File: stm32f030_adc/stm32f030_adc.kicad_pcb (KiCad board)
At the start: 2 copper layers, 35 parts, among them J4 Conn_01x05_Socket, Q1 BC337, U1 STM32F103C6Tx, U2 AMS1117-3.3, X1 USB_B_Micro, Y1 8 MHz

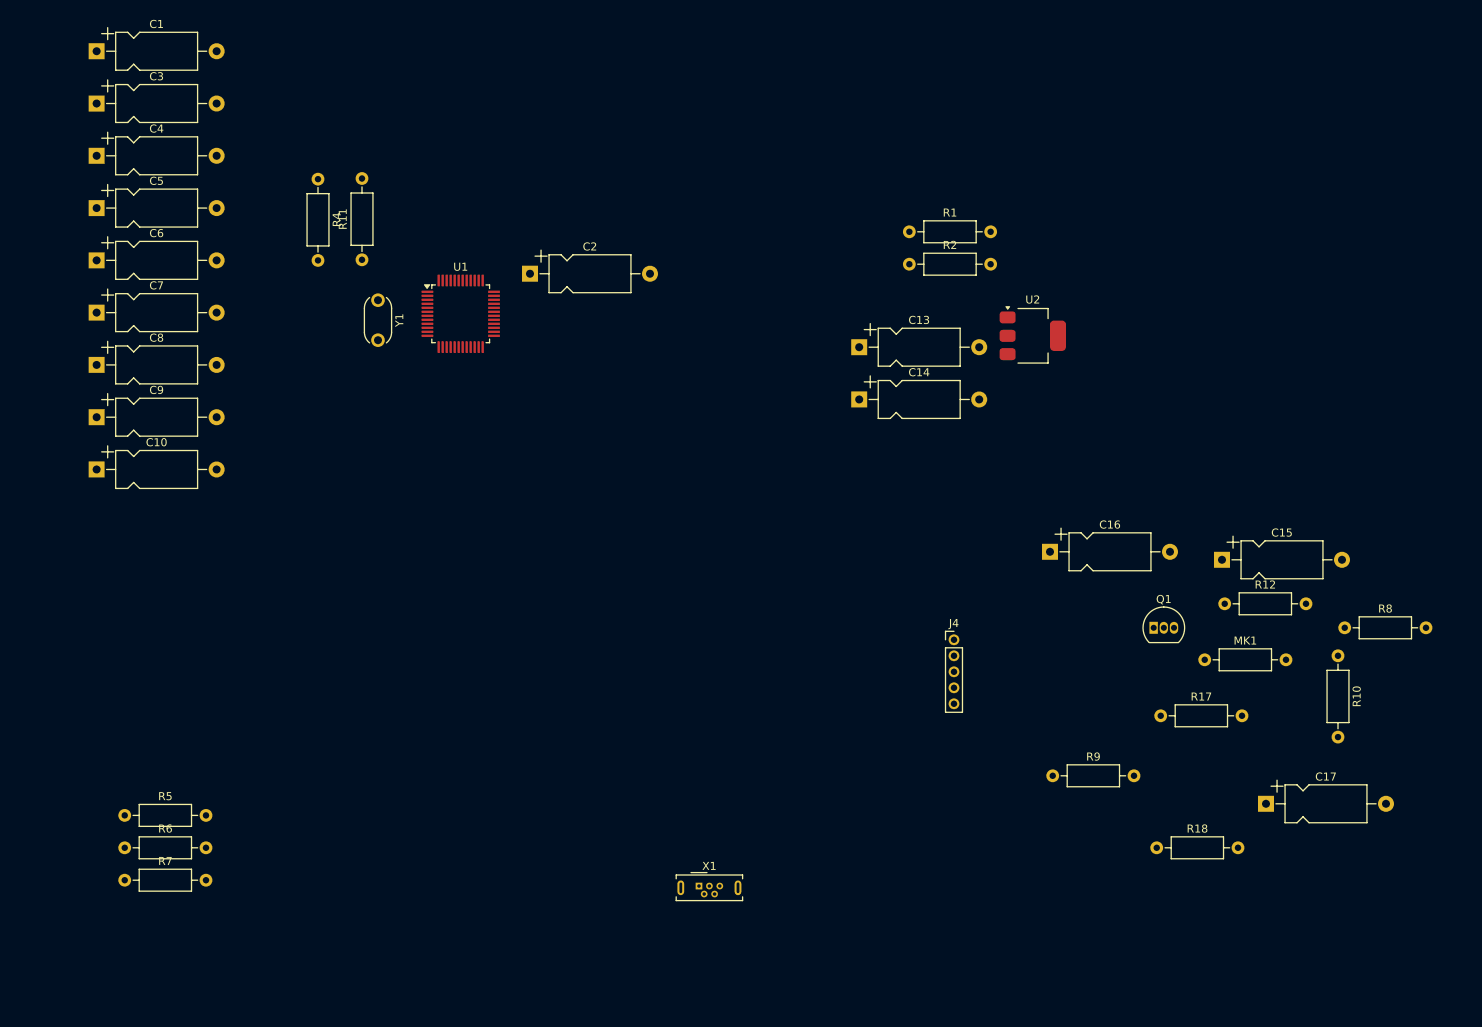
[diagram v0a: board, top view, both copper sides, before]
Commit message: [schematics] Build | Changed oscillator type, fixed unconnected lines, made some layout
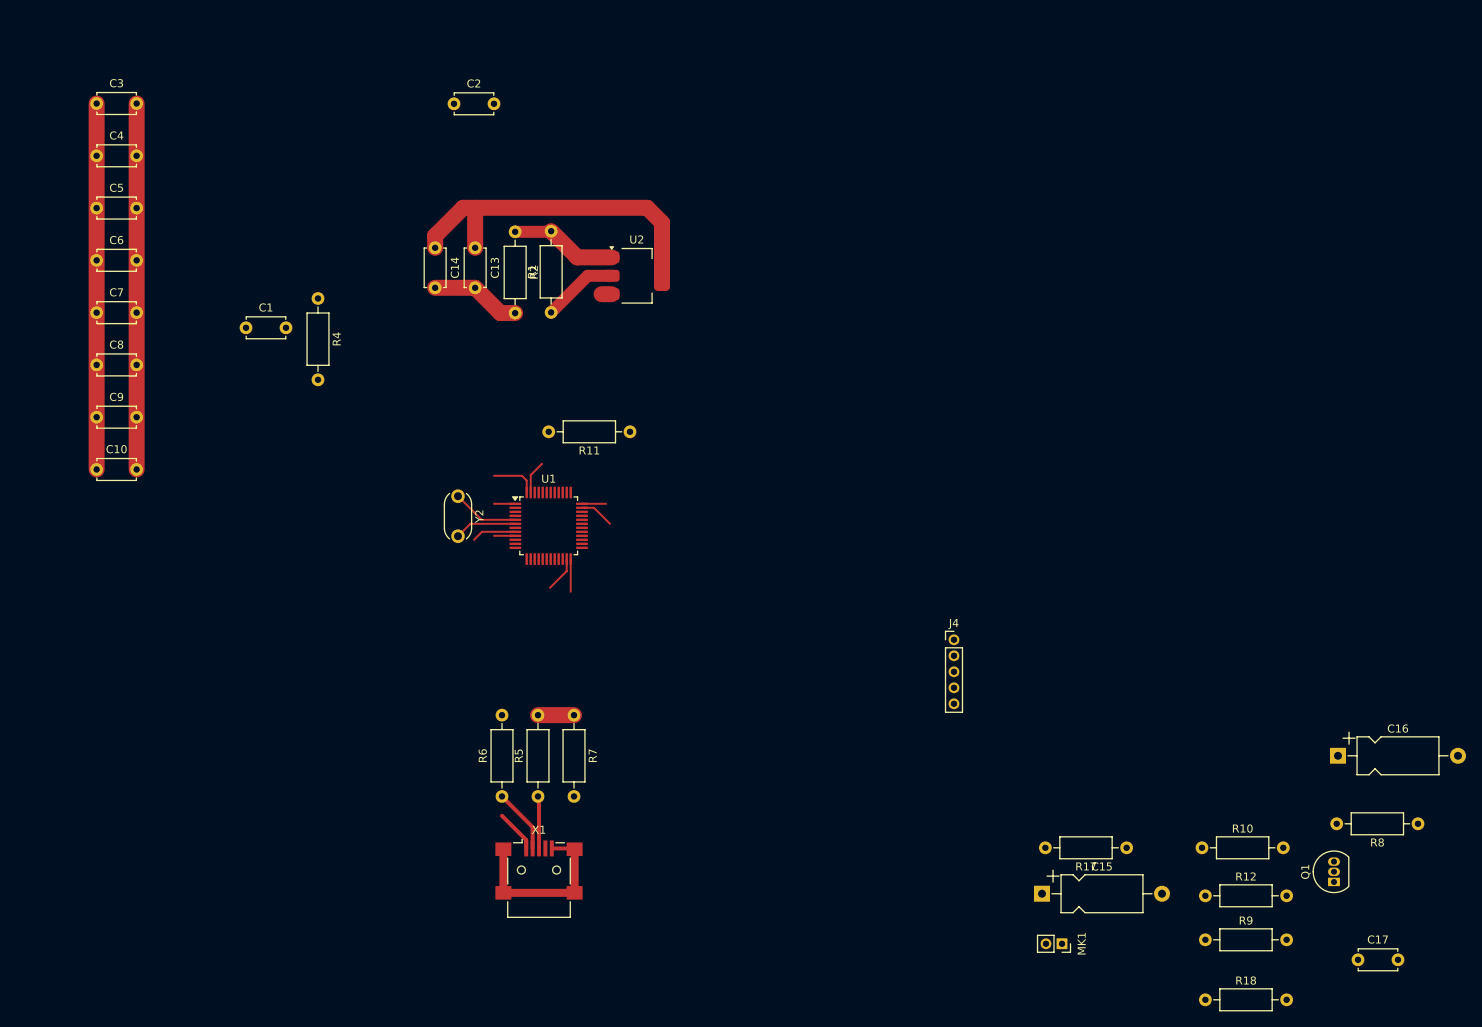
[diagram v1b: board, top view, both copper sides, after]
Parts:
- removed Y1: 8 MHz, Crystal:Resonator-2Pin_W6.0mm_H3.0mm
- added Y2: 8 MHz, Crystal:Resonator-2Pin_W6.0mm_H3.0mm, F.Cu at (142.0, 88.5)
- C1, C10, C13, C14, C17, C2, C3, C4, C5, C6, C7, C8, C9: footprint Capacitor_THT:CP_Axial_L10.0mm_D4.5mm_P15.00mm_Horizontal -> Capacitor_THT:C_Disc_D4.7mm_W2.5mm_P5.00mm
- MK1: footprint Resistor_THT:R_Axial_DIN0207_L6.3mm_D2.5mm_P10.16mm_Horizontal -> Connector_PinSocket_2.00mm:PinSocket_1x02_P2.00mm_Vertical
- X1: footprint Connector_USB:USB_Micro-B_Wuerth_614105150721_Vertical -> Connector_USB:USB_Mini-B_Lumberg_2486_01_Horizontal
- moved R7 59.8 mm to (156.5, 115.9), turned to -90 degrees
- moved C14 56.3 mm to (139.1, 57.5), turned to -90 degrees
- moved R5 51.7 mm to (152.0, 126.1), turned to 90 degrees
- moved U2 50.1 mm to (164.3, 61.0)
- moved C13 49.6 mm to (144.1, 57.5), turned to -90 degrees
- moved R2 49.4 mm to (149.1, 55.5), turned to -90 degrees
- moved R6 47.6 mm to (147.5, 126.1), turned to 90 degrees
- moved C15 47.4 mm to (215.0, 138.2)
- moved R1 45.9 mm to (153.6, 65.6), turned to 90 degrees
- moved C16 44.1 mm to (252.0, 121.0)
- moved R11 39.8 mm to (163.5, 80.5), turned to 180 degrees
- moved MK1 39.7 mm to (217.5, 144.5), turned to -90 degrees
- moved C1 39.3 mm to (115.5, 67.5)
- moved Q1 39.0 mm to (251.5, 136.8), turned to 90 degrees
- moved R12 36.6 mm to (235.4, 138.5)
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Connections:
- C13 pad 2: Net-(C13-Pad2) -> GNDREF
- C14 pad 2: Net-(C13-Pad2) -> GNDREF
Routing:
- net +3V3: track 0.00 -> 117.3 mm
- net GNDREF: track 0.00 -> 98.9 mm
- net Net-(U2-ADJ): track 0.00 -> 13.4 mm
- net Net-(U1-PD0): track 0.00 -> 8.40 mm
- net Net-(X1-D-): track 0.00 -> 8.08 mm
- net Net-(U1-PD1): track 0.00 -> 7.82 mm
- net 5V_USB: track 0.00 -> 6.58 mm
- net Net-(X1-D+): track 0.00 -> 6.55 mm
- net /Power and MCU/USB_D+: track 0.00 -> 4.50 mm

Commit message: [schematics] Impl |  Most of the work is done. Intermediate result
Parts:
- removed J4: Conn_01x05_Socket, Connector_PinHeader_2.00mm:PinHeader_1x05_P2.00mm_Vertical
- added J1: Conn_01x03_Socket, Connector_PinHeader_1.00mm:PinHeader_1x03_P1.00mm_Vertical, F.Cu at (148.0, 111.5)
- added TP1: TestPoint, TestPoint:TestPoint_Pad_D2.0mm, F.Cu at (155.0, 113.0)
- added TP2: TestPoint, TestPoint:TestPoint_Pad_D2.0mm, F.Cu at (157.8, 108.5)
- C15, C16: footprint Capacitor_THT:CP_Axial_L10.0mm_D4.5mm_P15.00mm_Horizontal -> Capacitor_THT:CP_Radial_D8.0mm_P3.80mm
- C17: footprint Capacitor_THT:C_Disc_D4.7mm_W2.5mm_P5.00mm -> Capacitor_THT:CP_Radial_D8.0mm_P3.80mm
- moved R8 136.1 mm to (127.8, 107.0)
- moved R12 119.2 mm to (117.6, 120.0)
- moved R18 119.2 mm to (117.6, 133.0)
- moved R9 119.2 mm to (117.6, 126.0)
- moved C16 118.7 mm to (134.7, 103.0)
- moved C17 117.3 mm to (138.2, 131.0), turned to 90 degrees
- moved Q1 117.2 mm to (135.7, 118.8)
- moved MK1 116.3 mm to (121.0, 79.5), turned to 0 degrees
- moved R10 109.0 mm to (127.7, 113.5), turned to 180 degrees
- moved R17 103.1 mm to (127.8, 100.0)
- moved C15 102.1 mm to (124.5, 91.0), turned to 180 degrees
- moved C3 85.2 mm to (172.2, 79.3)
- moved C5 81.6 mm to (172.2, 83.8)
- moved C10 79.0 mm to (172.0, 109.5)
- moved C7 79.0 mm to (172.0, 89.9)
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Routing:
- net GNDREF: track 98.9 -> 274.2 mm
- net +3V3: track 117.3 -> 242.8 mm
- net 5V_USB: track 6.58 -> 84.8 mm
- net Net-(Q1-B): track 0.00 -> 42.4 mm
- net Net-(MK1-+): track 0.00 -> 21.4 mm
- net Net-(Q1-C): track 0.00 -> 21.1 mm
- net Net-(U1-NRST): track 0.00 -> 21.1 mm
- net Net-(Q1-E): track 0.00 -> 20.8 mm
- net /Electret AMP/MIC_AMP_OUT: track 0.00 -> 14.1 mm
- net Net-(C17-Pad1): track 0.00 -> 11.2 mm
- net /Power and MCU/USB_D-: track 0.00 -> 9.67 mm
- net /Power and MCU/USART_1_TX: track 0.00 -> 7.09 mm
- net /Power and MCU/USB_D+: track 4.50 -> 10.9 mm
- net /Power and MCU/USART_1_RX: track 0.00 -> 6.30 mm
- net Net-(U1-BOOT0): track 0.00 -> 5.40 mm
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
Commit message: Layout: cleaner version (intermediate)
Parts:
- moved R11 92.3 mm to (215.4, 39.7), turned to 0 degrees
- moved R4 90.4 mm to (215.4, 35.6), turned to 0 degrees
- moved C4 85.4 mm to (207.2, 47.8), turned to 0 degrees
- moved C1 81.1 mm to (207.2, 35.6), turned to 0 degrees
- moved C6 77.1 mm to (207.2, 55.9), turned to 0 degrees
- moved C2 73.5 mm to (207.2, 39.7), turned to 0 degrees
- moved C10 51.4 mm to (207.2, 72.1)
- moved U2 50.6 mm to (152.0, 124.2)
- moved C3 50.0 mm to (207.2, 43.8)
- moved C9 49.6 mm to (207.2, 68.0)
- moved C8 47.9 mm to (207.2, 64.0)
- moved C5 47.5 mm to (207.2, 51.9)
- moved C7 46.3 mm to (207.2, 60.0)
- moved R2 45.8 mm to (146.2, 113.7), turned to 0 degrees
- moved C13 44.3 mm to (156.2, 109.4), turned to 180 degrees
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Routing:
- net GNDREF: track 274.2 -> 88.2 mm
- net +3V3: track 242.8 -> 88.0 mm
- net 5V_USB: track 84.8 -> 6.72 mm
- net /Power and MCU/USB_D+: track 10.9 -> 34.4 mm
- net Net-(U1-NRST): track 21.1 -> 0.00 mm
- net /Power and MCU/USB_D-: track 9.67 -> 26.7 mm
- net /Electret AMP/MIC_AMP_OUT: track 14.1 -> 0.00 mm
- net Net-(X1-D+): track 6.38 -> 18.7 mm
- net Net-(X1-D-): track 8.08 -> 15.3 mm
- net /Power and MCU/USART_1_TX: track 7.09 -> 0.00 mm
- net /Power and MCU/USART_1_RX: track 6.30 -> 0.00 mm
- net Net-(U1-PD1): track 11.3 -> 5.46 mm
- net Net-(U1-BOOT0): track 5.40 -> 0.00 mm
- net Net-(U2-ADJ): track 13.4 -> 9.39 mm
- net /Power and MCU/SWD_CLK: track 2.50 -> 5.36 mm
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
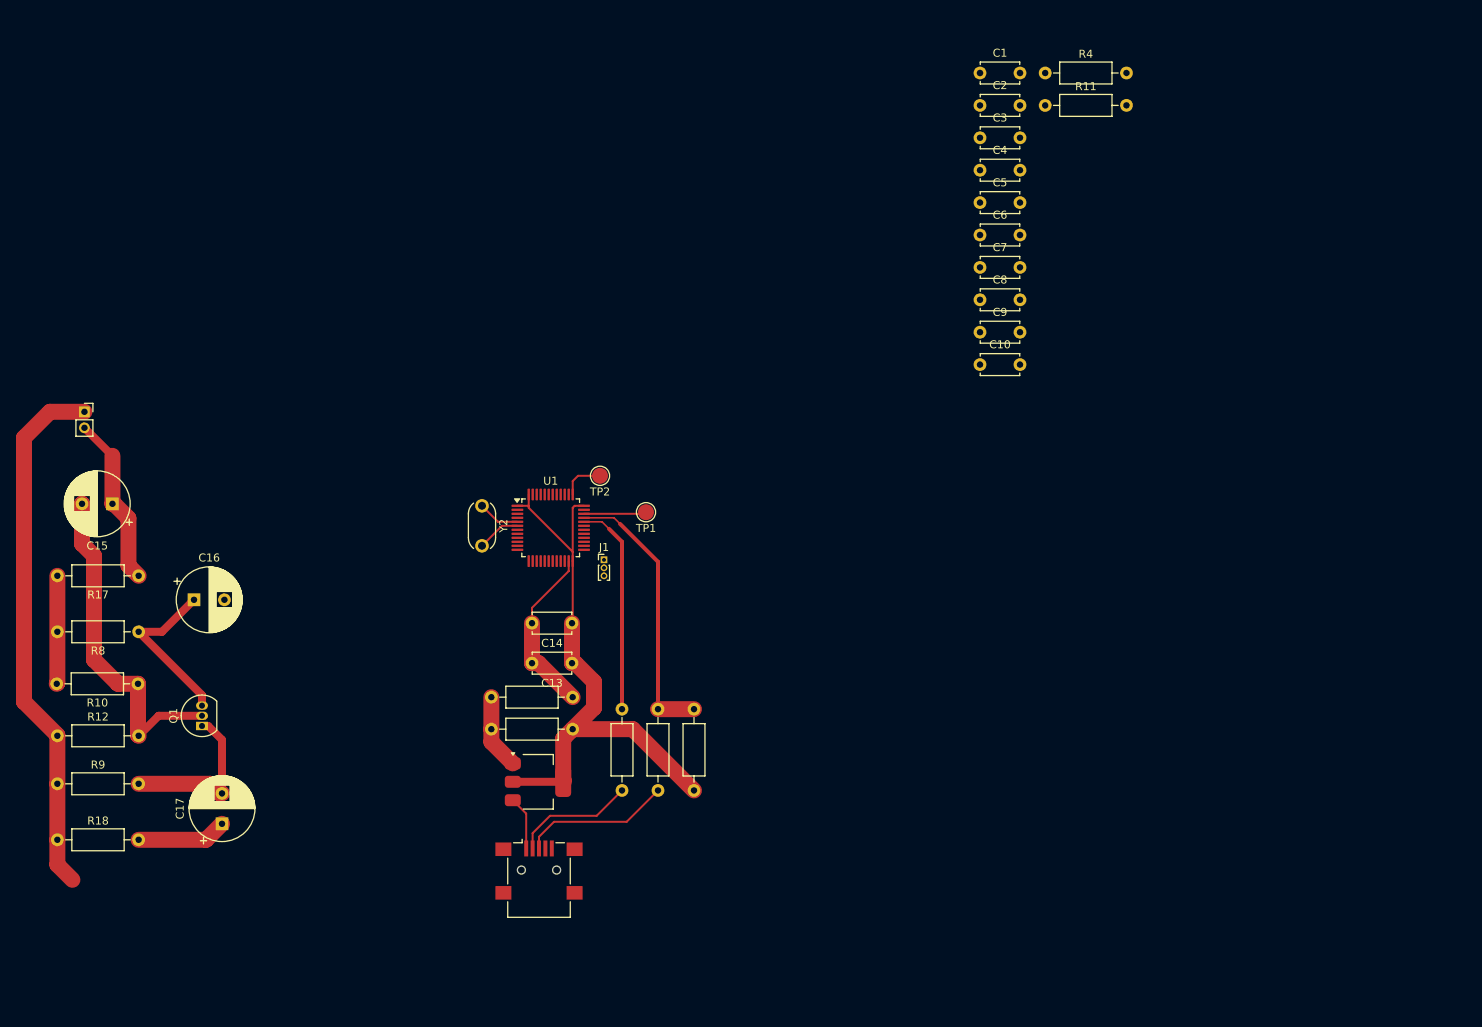
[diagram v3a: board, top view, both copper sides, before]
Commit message: Layout: 1-layer board, done, first approximation
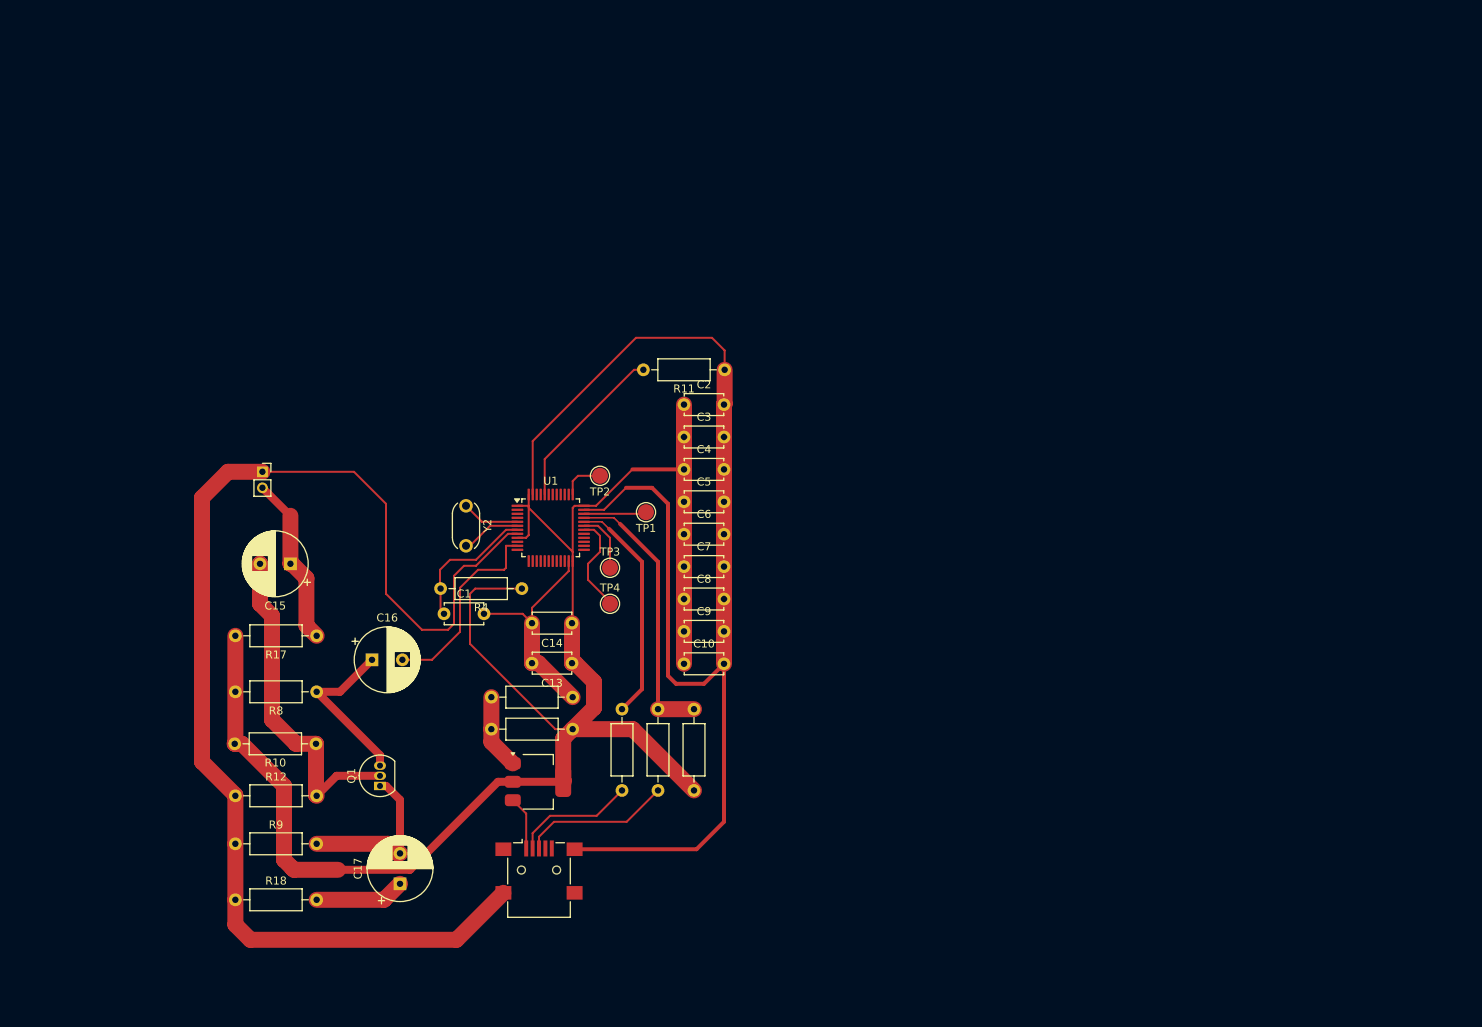
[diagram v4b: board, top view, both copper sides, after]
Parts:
- removed J1: Conn_01x03_Socket, Connector_PinHeader_1.00mm:PinHeader_1x03_P1.00mm_Vertical
- added TP3: TestPoint, TestPoint:TestPoint_Pad_D2.0mm, F.Cu at (161.0, 97.5)
- added TP4: TestPoint, TestPoint:TestPoint_Pad_D2.0mm, F.Cu at (161.0, 102.0)
- moved C1 95.2 mm to (140.2, 103.2)
- moved R4 91.8 mm to (150.0, 100.1), turned to 180 degrees
- moved C10 52.6 mm to (170.2, 109.5)
- moved C3 52.6 mm to (170.2, 81.2)
- moved C4 52.6 mm to (170.2, 85.2)
- moved C5 52.6 mm to (170.2, 89.2)
- moved C6 52.6 mm to (170.2, 93.3)
- moved C8 52.6 mm to (170.2, 101.4)
- moved C9 52.6 mm to (170.2, 105.5)
- moved C2 52.6 mm to (170.2, 77.1)
- moved C7 52.6 mm to (170.2, 97.3)
- moved R11 51.9 mm to (175.3, 72.8), turned to 180 degrees
- moved C15 23.5 mm to (121.1, 97.0)
- moved C16 23.5 mm to (131.2, 109.0)
- moved C17 23.5 mm to (134.8, 137.0)
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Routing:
- net GNDREF: track 88.2 -> 342.0 mm
- net +3V3: track 88.0 -> 221.2 mm
- net /Electret AMP/MIC_AMP_OUT: track 0.00 -> 25.1 mm
- net Net-(U1-BOOT0): track 0.00 -> 21.4 mm
- net Net-(U1-NRST): track 0.00 -> 17.5 mm
- net /Power and MCU/USART_1_TX: track 0.00 -> 12.6 mm
- net /Power and MCU/USART_1_RX: track 0.00 -> 7.62 mm
- net /Power and MCU/USB_D-: track 26.7 -> 28.8 mm
- net Net-(U1-PD1): track 5.46 -> 7.46 mm
- net Net-(U1-PD0): track 5.25 -> 7.25 mm
